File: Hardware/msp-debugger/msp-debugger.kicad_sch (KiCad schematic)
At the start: 23 parts, among them J1 USB_B_Micro, J2 Conn_02x10, U1 ESP32-S2-SOLO, U2 NHD-0420H1Z, U3 BA033CC0FP-E2

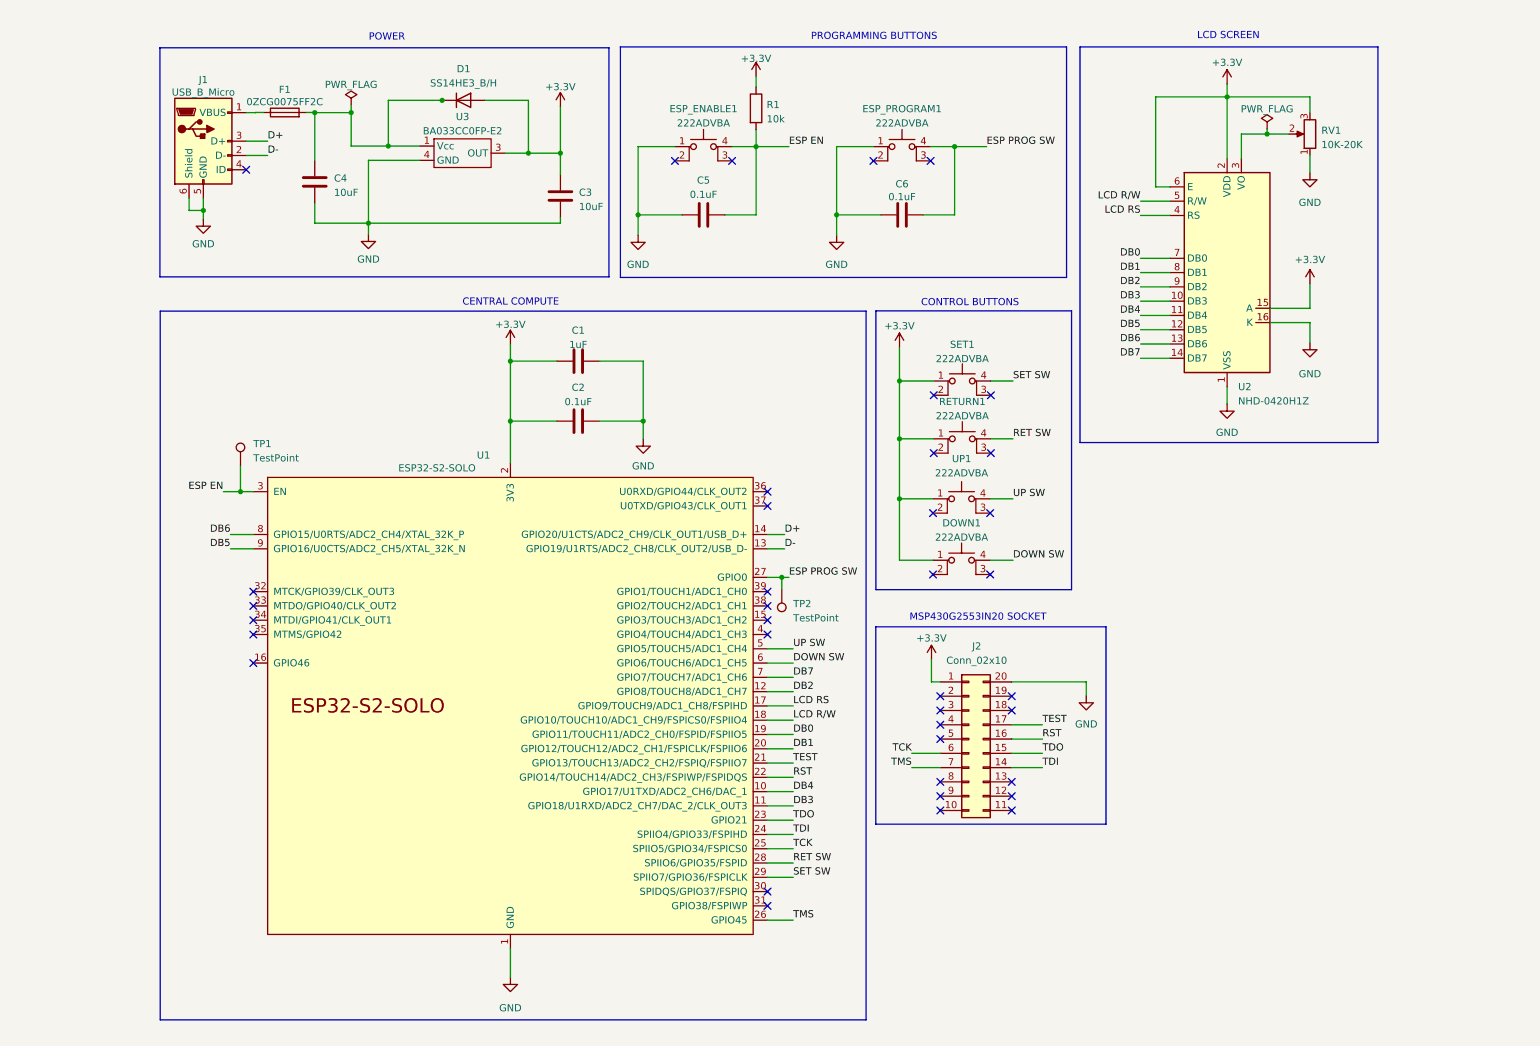
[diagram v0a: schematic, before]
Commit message: begin updating pcb with g2553
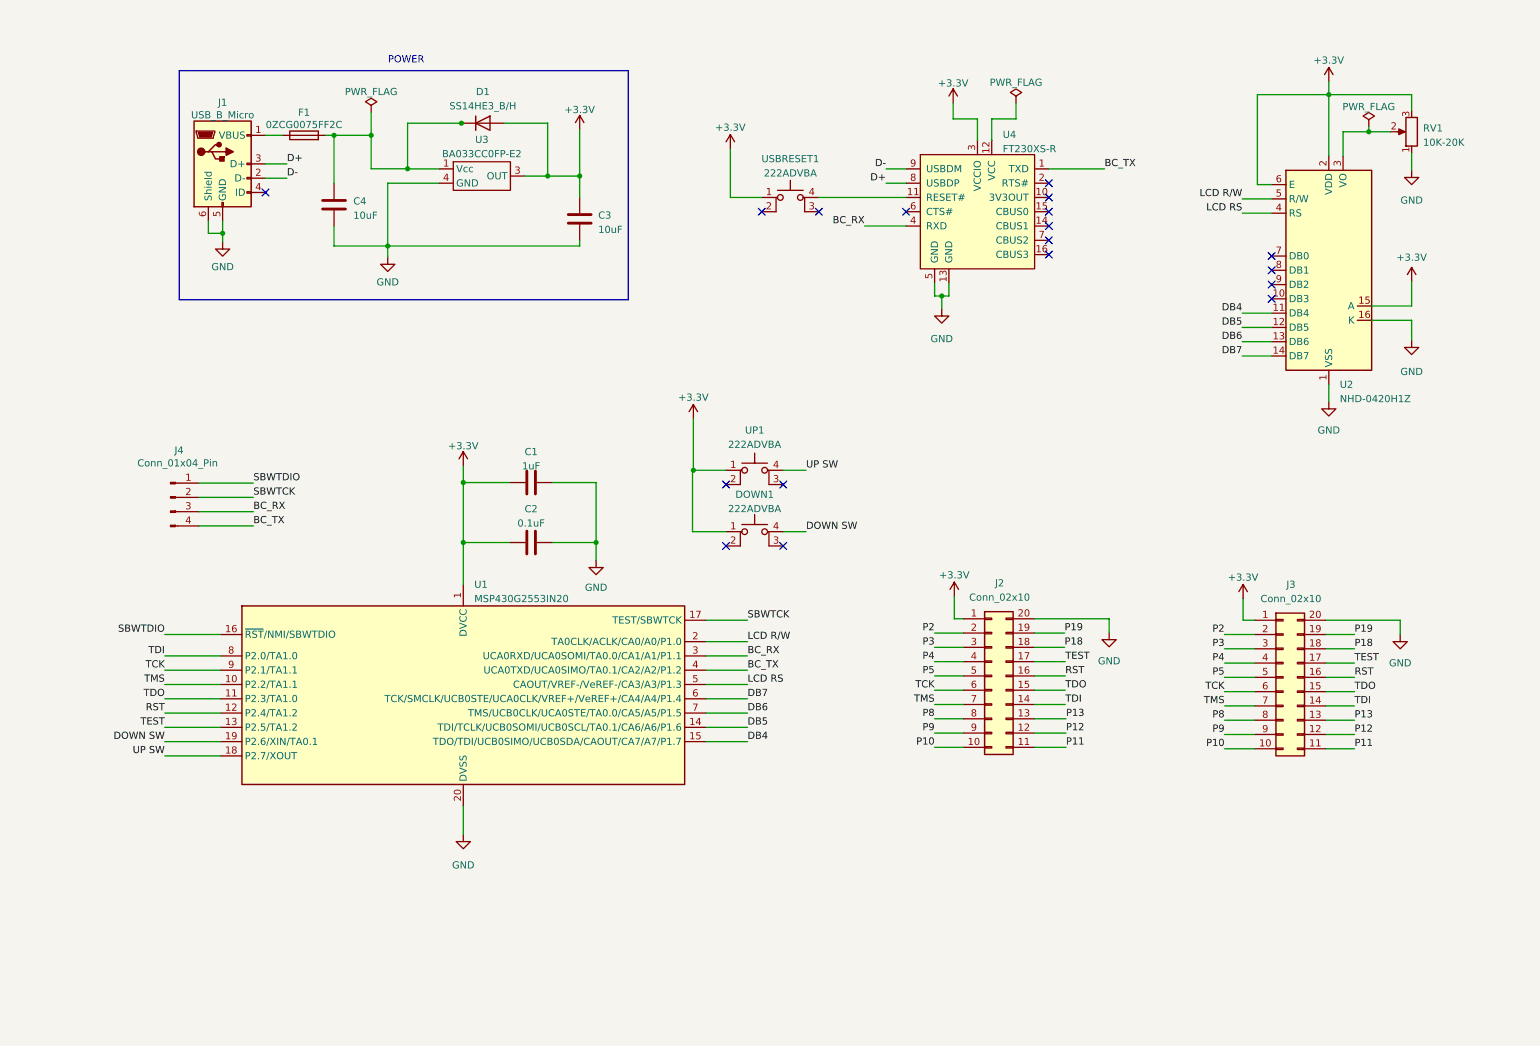
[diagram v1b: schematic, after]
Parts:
- removed C5, C6: 0.1uF, Capacitor_SMD:C_0805_2012Metric, symbol Device:C
- removed ESP_ENABLE1, ESP_PROGRAM1, RETURN1, SET1: 222ADVBA, buttons:SW_222ADVBA, symbol Switch:SW_MEC_5E
- removed R1: 10k, Resistor_SMD:R_0805_2012Metric, symbol Device:R
- removed TP1, TP2: TestPoint, TestPoint:TestPoint_Pad_1.5x1.5mm, symbol Connector:TestPoint
- removed U1: ESP32-S2-SOLO, Espressif:ESP32-S2-SOLO, symbol Espressif:ESP32-S2-SOLO
- added J3: Conn_02x10, Connector_PinHeader_2.54mm:PinHeader_2x10_P2.54mm_Vertical, symbol Connector_Generic:Conn_02x10_Counter_Clockwise
- added J4: Conn_01x04_Pin, Connector_PinHeader_2.54mm:PinHeader_1x04_P2.54mm_Vertical, symbol Connector:Conn_01x04_Pin
- added U1: MSP430G2553IN20, Package_DIP:DIP-20_W7.62mm, symbol MCU_Texas_MSP430:MSP430G2553IN20
- added U4: FT230XS-R, digikey-footprints:SOIC-16_W3.90mm, symbol dk_Interface-Controllers:FT230XS-R
- added USBRESET1: 222ADVBA, buttons:SW_222ADVBA, symbol Switch:SW_MEC_5E
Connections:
- net +3.3V: now also J3.1 (Pin_1), U1.1 (DVCC), U4.3 (VCCIO), USBRESET1.1
- net D+: now also U4.8 (USBDP)
- net D-: now also U4.9 (USBDM)
- net DB4: now also U1.15 (TDO/TDI/UCB0SIMO/UCB0SDA/CAOUT/CA7/A7/P1.7)
- net DB5: now also U1.14 (TDI/TCLK/UCB0SOMI/UCB0SCL/TA0.1/CA6/A6/P1.6)
- net DB6: now also U1.7 (TMS/UCB0CLK/UCA0STE/TA0.0/CA5/A5/P1.5)
- net DB7: now also U1.6 (TCK/SMCLK/UCB0STE/UCA0CLK/VREF+/VeREF+/CA4/A4/P1.4)
- net DOWN SW: now also U1.19 (P2.6/XIN/TA0.1)
- net GND: now also J3.20 (Pin_20), U1.20 (DVSS), U4.13 (GND), U4.5 (GND)
- net LCD RS: now also U1.5 (CAOUT/VREF-/VeREF-/CA3/A3/P1.3)
- net LCD R/W: now also U1.2 (TA0CLK/ACLK/CA0/A0/P1.0)
- net RST: now also J3.16 (Pin_16), U1.12 (P2.4/TA1.2)
- net TCK: now also J3.6 (Pin_6), U1.9 (P2.1/TA1.1)
- net TDI: now also J3.14 (Pin_14), U1.8 (P2.0/TA1.0)
- net TDO: now also J3.15 (Pin_15), U1.11 (P2.3/TA1.0)
- net TEST: now also J3.17 (Pin_17), U1.13 (P2.5/TA1.2)
- net TMS: now also J3.7 (Pin_7), U1.10 (P2.2/TA1.1)
- net UP SW: now also U1.18 (P2.7/XOUT)
- net P10: now reaches J2.10 (Pin_10)
- net P10: now also J3.10 (Pin_10)
- net P11: now reaches J2.11 (Pin_11)
- net P11: now also J3.11 (Pin_11)
- net P12: now reaches J2.12 (Pin_12)
- net P12: now also J3.12 (Pin_12)
- net P13: now reaches J2.13 (Pin_13)
- net P13: now also J3.13 (Pin_13)
- net P18: now reaches J2.18 (Pin_18)
- net P18: now also J3.18 (Pin_18)
- net P19: now reaches J2.19 (Pin_19)
- net P19: now also J3.19 (Pin_19)
- net P2: now reaches J2.2 (Pin_2)
- net P2: now also J3.2 (Pin_2)
- net P3: now reaches J2.3 (Pin_3)
- net P3: now also J3.3 (Pin_3)
- net P4: now reaches J2.4 (Pin_4)
- net P4: now also J3.4 (Pin_4)
- net P5: now reaches J2.5 (Pin_5)
- net P5: now also J3.5 (Pin_5)
- net P8: now reaches J2.8 (Pin_8)
- net P8: now also J3.8 (Pin_8)
- net P9: now reaches J2.9 (Pin_9)
- net P9: now also J3.9 (Pin_9)
- net DB0: no longer names the net of U2.7 (DB0)
- net DB1: no longer names the net of U2.8 (DB1)
- net DB2: no longer names the net of U2.9 (DB2)
- net DB3: no longer names the net of U2.10 (DB3)
- new net: U4.11 (RESET#), USBRESET1.4 (A)
- new net BC_RX: J4.3 (Pin_3), U1.3 (UCA0RXD/UCA0SOMI/TA0.0/CA1/A1/P1.1), U4.4 (RXD)
- new net BC_TX: J4.4 (Pin_4), U1.4 (UCA0TXD/UCA0SIMO/TA0.1/CA2/A2/P1.2), U4.1 (TXD)
- new net SBWTCK: J4.2 (Pin_2), U1.17 (TEST/SBWTCK)
- new net SBWTDIO: J4.1 (Pin_1), U1.16 (~{RST}/NMI/SBWTDIO)
- no-connect marks 38 -> 18
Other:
- note removed: "CENTRAL COMPUTE"
- note removed: "CONTROL BUTTONS"
- note removed: "LCD SCREEN"
- note removed: "MSP430G2553IN20 SOCKET"
- note removed: "PROGRAMMING BUTTONS"
- moved on the sheet: C1, C2, C3, C4, D1, DOWN1, F1, J1, J2, RV1, U2, U3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

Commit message: route new pcb
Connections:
- net +5V: now reaches C4.1, D1.1 (K), F1.2, U3.1 (Vcc)
- net +5V: now also U4.12 (VCC)
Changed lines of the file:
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@@
   (junction (at 248.412 29.21) (diameter 0) (color 0 0 0 0)
+  )
+  (junction (at 86.995 34.29) (diameter 0) (color 0 0 0 0)
   )
   (junction (at 94.488 108.8644) (diameter 0) (color 0 0 0 0)
@@
     (stroke (width 0) (type default))
   )
+  (wire (pts (xy 192.024 33.528) (xy 192.024 30.734))
+    (stroke (width 0) (type default))
+  )
   (wire (pts (xy 59.309 44.069) (xy 63.119 44.069))
     (stroke (width 0) (type default))
@@
     (stroke (width 0) (type default))
   )
-  (wire (pts (xy 192.786 33.528) (xy 188.468 33.528))
-    (stroke (width 0) (type default))
-  )
   (wire (pts (xy 137.668 134.112) (xy 145.034 134.112))
     (stroke (width 0) (type default))
@@
     (stroke (width 0) (type default))
   )
-  (wire (pts (xy 192.786 30.734) (xy 192.786 33.528))
-    (stroke (width 0) (type default))
-  )
   (wire (pts (xy 165.862 52.578) (xy 173.228 52.578))
     (stroke (width 0) (type default))
@@
     (stroke (width 0) (type default))
   )
+  (wire (pts (xy 188.468 33.528) (xy 192.024 33.528))
+    (stroke (width 0) (type default))
+  )
   (wire (pts (xy 235.204 122.682) (xy 233.172 122.682))
     (stroke (width 0) (type default))
@@
     (stroke (width 0) (type default))
   )
+  (wire (pts (xy 188.468 37.338) (xy 188.468 33.528))
+    (stroke (width 0) (type default))
+  )
   (wire (pts (xy 137.668 144.272) (xy 145.034 144.272))
     (stroke (width 0) (type default))
@@
     (stroke (width 0) (type default))
   )
-  (wire (pts (xy 188.468 33.528) (xy 188.468 37.338))
-    (stroke (width 0) (type default))
-  )
   (wire (pts (xy 94.488 108.8644) (xy 102.743 108.8644))
     (stroke (width 0) (type default))
@@
     (stroke (width 0) (type default))
   )
+  (wire (pts (xy 86.995 34.29) (xy 94.1578 34.29))
+    (stroke (width 0) (type default))
+  )
   (wire (pts (xy 229.87 125.222) (xy 235.204 125.222))
     (stroke (width 0) (type default))
@@
     (stroke (width 0) (type default))
   )
+  (wire (pts (xy 86.995 32.385) (xy 86.995 34.29))
+    (stroke (width 0) (type default))
+  )
   (wire (pts (xy 135.255 106.934) (xy 135.255 96.012))
     (stroke (width 0) (type default))
@@
     (stroke (width 0) (type default))
   )
-  (wire (pts (xy 84.582 34.29) (xy 94.1578 34.29))
+  (wire (pts (xy 84.582 34.29) (xy 86.995 34.29))
     (stroke (width 0) (type default))
   )
@@
     )
   )
-  (symbol (lib_id "power:PWR_FLAG") (at 192.786 30.734 0) (unit 1)
-    (in_bom yes) (on_board yes) (dnp no) (fields_autoplaced)
-    (property "Reference" "#FLG02" (at 192.786 28.829 0)
-      (effects (font (size 1.27 1.27)) hide)
-    )
-    (property "Value" "PWR_FLAG" (at 192.786 27.051 0)
-      (effects (font (size 1.27 1.27)))
-    )
-    (property "Footprint" "" (at 192.786 30.734 0)
-      (effects (font (size 1.27 1.27)) hide)
-    )
-    (property "Datasheet" "~" (at 192.786 30.734 0)
-      (effects (font (size 1.27 1.27)) hide)
-    )
-    (pin "1")
-    (instances
-      (project "msp-debugger"
-        (path "/045ba461-bcb4-4373-9dc5-687bfd2826ef"
-          (reference "#FLG02") (unit 1)
-        )
-      )
-    )
-  )
   (symbol (lib_id "Device:C") (at 115.189 51.308 0) (unit 1)
     (in_bom yes) (on_board yes) (dnp no) (fields_autoplaced)
@@
     )
   )
+  (symbol (lib_id "power:+5V") (at 192.024 30.734 0) (unit 1)
+    (in_bom yes) (on_board yes) (dnp no) (fields_autoplaced)
+    (property "Reference" "#PWR019" (at 192.024 34.544 0)
+      (effects (font (size 1.27 1.27)) hide)
+    )
+    (property "Value" "+5V" (at 192.024 26.924 0)
+      (effects (font (size 1.27 1.27)))
+    )
+    (property "Footprint" "" (at 192.024 30.734 0)
+      (effects (font (size 1.27 1.27)) hide)
+    )
+    (property "Datasheet" "" (at 192.024 30.734 0)
+      (effects (font (size 1.27 1.27)) hide)
+    )
+    (pin "1")
+    (instances
+      (project "msp-debugger"
+        (path "/045ba461-bcb4-4373-9dc5-687bfd2826ef"
+          (reference "#PWR019") (unit 1)
+        )
+      )
+    )
+  )
   (symbol (lib_id "power:GND") (at 209.3468 124.8664 0) (unit 1)
     (in_bom yes) (on_board yes) (dnp no) (fields_autoplaced)
@@
         )
       )
+    )
+  )
+  (symbol (lib_id "power:+5V") (at 86.995 32.385 0) (unit 1)
+    (in_bom yes) (on_board yes) (dnp no) (fields_autoplaced)
+    (property "Reference" "#PWR018" (at 86.995 36.195 0)
+      (effects (font (size 1.27 1.27)) hide)
+    )
+    (property "Value" "+5V" (at 86.995 28.575 0)
+      (effects (font (size 1.27 1.27)))
+    )
+    (property "Footprint" "" (at 86.995 32.385 0)
+      (effects (font (size 1.27 1.27)) hide)
+    )
+    (property "Datasheet" "" (at 86.995 32.385 0)
+      (effects (font (size 1.27 1.27)) hide)
+    )
+    (pin "1")
+    (instances
+      (project "msp-debugger"
+        (path "/045ba461-bcb4-4373-9dc5-687bfd2826ef"
+          (reference "#PWR018") (unit 1)
+        )
+      )
